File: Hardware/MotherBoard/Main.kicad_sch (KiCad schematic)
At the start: 15 parts, among them J9 Conn_02x02_Odd_Even, SW1 SW_Push, U2 28C256, U3 WD65C22, U4 HM62256BLP, U5 WD65C02, X1 ACO-1MHz

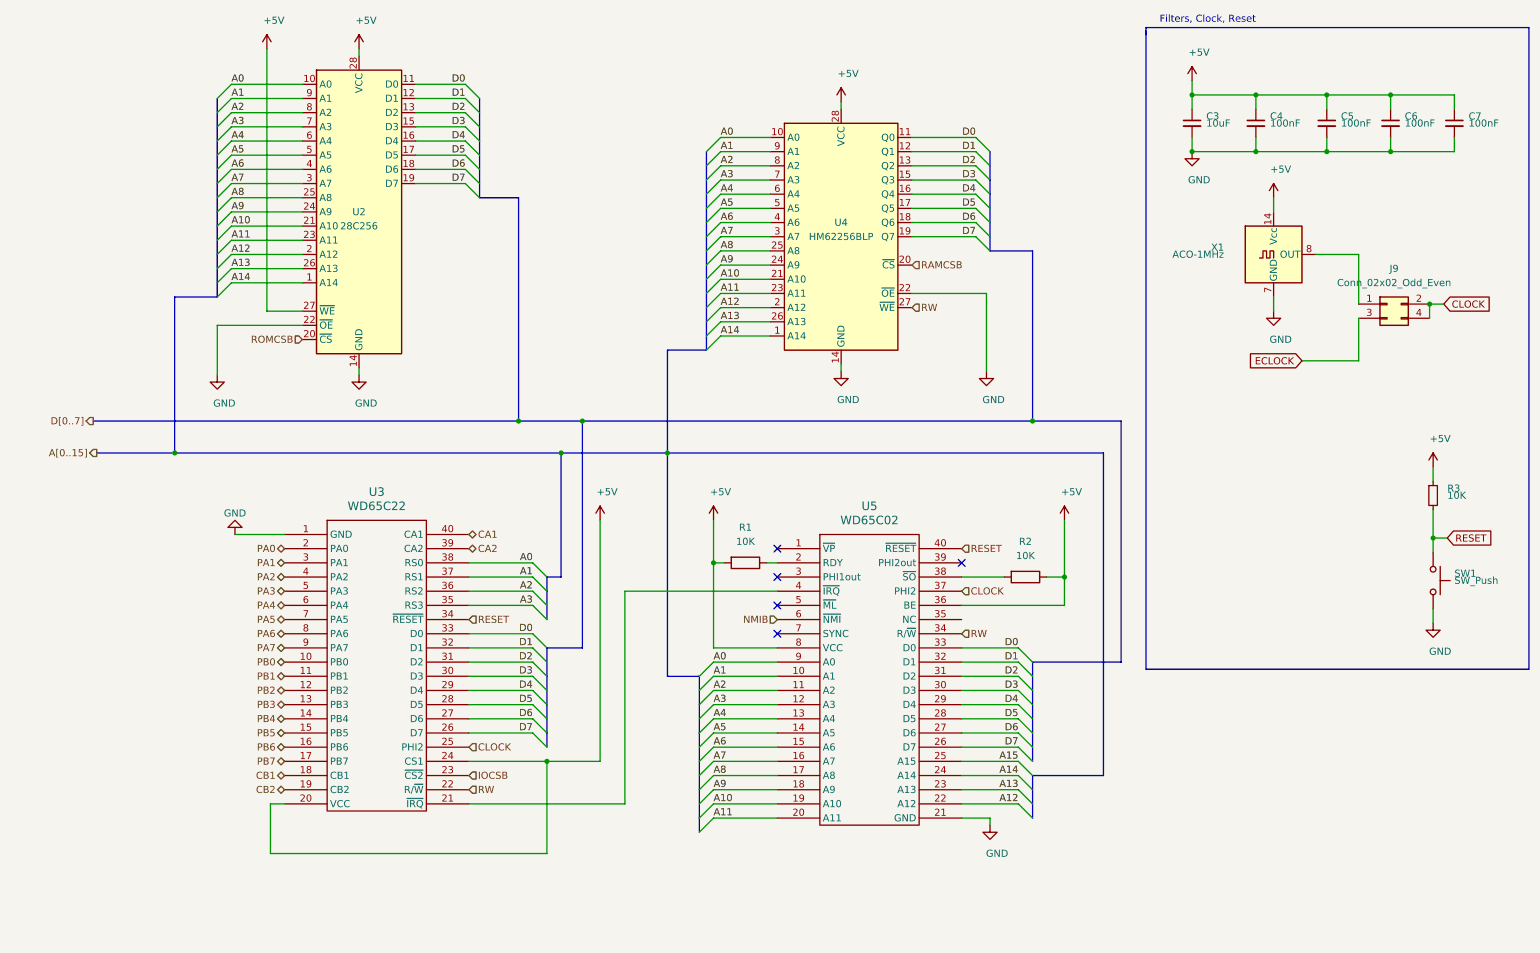
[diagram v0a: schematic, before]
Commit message: Add buffers to extenstion ports
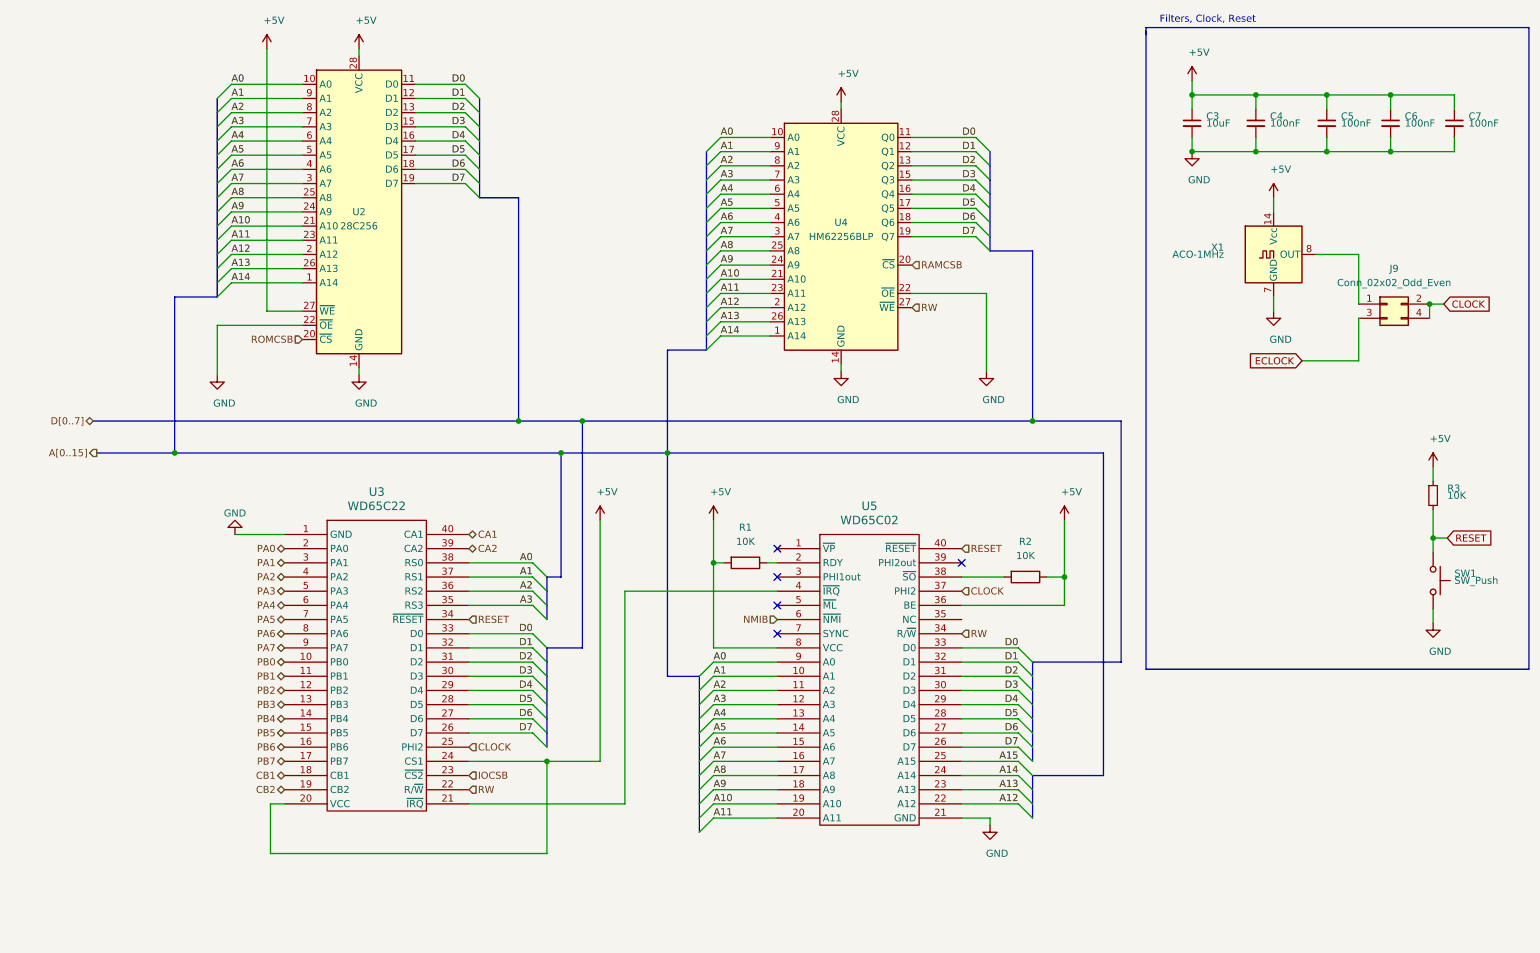
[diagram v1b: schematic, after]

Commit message: Fix
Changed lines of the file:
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@@
   (junction (at 128.905 92.71) (diameter 1.016) (color 0 0 0 0))
   (junction (at 194.31 86.995) (diameter 1.016) (color 0 0 0 0))
+  (no_connect (at 148.59 114.935))
+  (no_connect (at 181.61 112.395))
   (no_connect (at 148.59 125.095))
-  (no_connect (at 181.61 112.395))
   (no_connect (at 148.59 120.015))
   (no_connect (at 148.59 109.855))
-  (no_connect (at 148.59 114.935))
   (bus_entry (at 48.26 29.21) (size 2.54 -2.54)
     (stroke (width 0.1524) (type solid) (color 0 0 0 0))
@@
     (stroke (width 0) (type solid) (color 0 0 0 0))
   )
-  (wire (pts (xy 242.57 76.2) (xy 252.73 76.2))
-    (stroke (width 0) (type solid) (color 0 0 0 0))
-  )
   (wire (pts (xy 245.11 57.15) (xy 252.73 57.15))
     (stroke (width 0) (type solid) (color 0 0 0 0))
@@
     (stroke (width 0) (type solid) (color 0 0 0 0))
   )
+  (wire (pts (xy 252.73 76.2) (xy 267.97 76.2))
+    (stroke (width 0) (type solid) (color 0 0 0 0))
+  )
   (wire (pts (xy 258.445 28.575) (xy 269.875 28.575))
     (stroke (width 0) (type solid) (color 0 0 0 0))
@@
   (label "A12" (at 191.77 155.575 180)
     (effects (font (size 1.27 1.27)) (justify right bottom))
-  )
-  (global_label "ECLOCK" (shape input) (at 242.57 76.2 180)
-    (effects (font (size 1.27 1.27)) (justify right))
-  )
-  (global_label "CLOCK" (shape input) (at 267.97 66.04 0)
-    (effects (font (size 1.27 1.27)) (justify left))
-  )
-  (global_label "RESET" (shape input) (at 268.605 107.95 0)
-    (effects (font (size 1.27 1.27)) (justify left))
   )
   (hierarchical_label "D[0..7]" (shape bidirectional) (at 26.035 86.995 180)
@@
     (effects (font (size 1.27 1.27)) (justify left))
   )
+  (hierarchical_label "CLOCK" (shape input) (at 267.97 66.04 0)
+    (effects (font (size 1.27 1.27)) (justify left))
+  )
+  (hierarchical_label "ECLOCK" (shape input) (at 267.97 76.2 0)
+    (effects (font (size 1.27 1.27)) (justify left))
+  )
+  (hierarchical_label "RESET" (shape input) (at 268.605 107.95 0)
+    (effects (font (size 1.27 1.27)) (justify left))
+  )

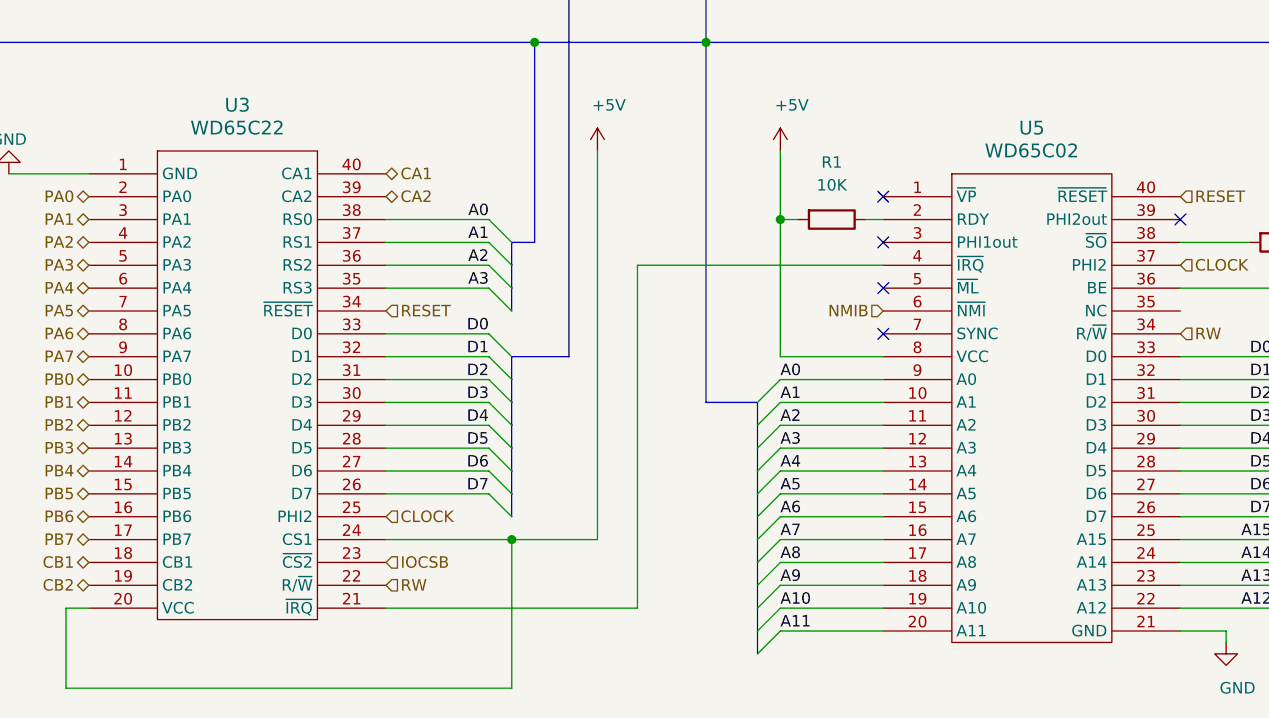
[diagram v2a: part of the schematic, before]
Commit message: Replace logic IC 4xxx by 74hcxx
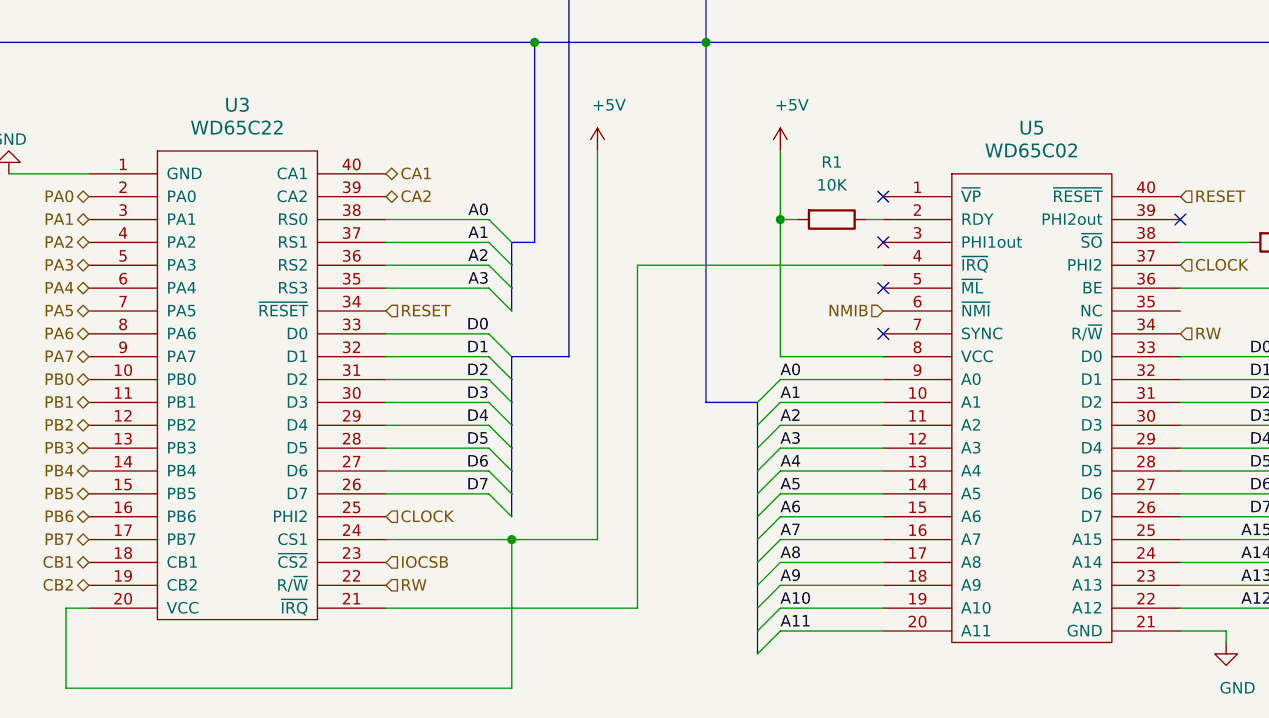
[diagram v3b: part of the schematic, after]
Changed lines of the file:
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@@
   (junction (at 128.905 92.71) (diameter 1.016) (color 0 0 0 0))
   (junction (at 194.31 86.995) (diameter 1.016) (color 0 0 0 0))
+  (no_connect (at 148.59 125.095))
+  (no_connect (at 148.59 109.855))
+  (no_connect (at 181.61 112.395))
   (no_connect (at 148.59 114.935))
-  (no_connect (at 181.61 112.395))
-  (no_connect (at 148.59 125.095))
   (no_connect (at 148.59 120.015))
-  (no_connect (at 148.59 109.855))
   (bus_entry (at 48.26 29.21) (size 2.54 -2.54)
     (stroke (width 0.1524) (type solid) (color 0 0 0 0))

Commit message: Finalize daughter board
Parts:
- added C8: 470nF, Capacitor_THT:C_Disc_D5.0mm_W2.5mm_P2.50mm, symbol Device:C_Small
- SW1: value SW_Push -> RESET_SW
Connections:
- net GND: now also C8.2
- net RESET: now also C8.1
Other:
- moved on the sheet: J9, X1
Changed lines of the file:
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@@
 (kicad_sch (version 20201015) (generator eeschema)
-  (page 1 4)
   (paper "A4")
   (title_block
@@
   (junction (at 258.445 28.575) (diameter 1.016) (color 0 0 0 0))
   (junction (at 258.445 38.735) (diameter 1.016) (color 0 0 0 0))
-  (junction (at 265.43 66.04) (diameter 1.016) (color 0 0 0 0))
   (junction (at 266.065 107.95) (diameter 1.016) (color 0 0 0 0))
+  (junction (at 266.065 121.92) (diameter 1.016) (color 0 0 0 0))
+  (junction (at 266.7 71.755) (diameter 1.016) (color 0 0 0 0))
   (junction (at 40.64 92.71) (diameter 1.016) (color 0 0 0 0))
   (junction (at 102.235 86.995) (diameter 1.016) (color 0 0 0 0))
@@
     (stroke (width 0) (type solid) (color 0 0 0 0))
   )
-  (wire (pts (xy 237.49 46.99) (xy 237.49 49.53))
-    (stroke (width 0) (type solid) (color 0 0 0 0))
-  )
-  (wire (pts (xy 237.49 64.77) (xy 237.49 67.31))
-    (stroke (width 0) (type solid) (color 0 0 0 0))
-  )
-  (wire (pts (xy 245.11 57.15) (xy 252.73 57.15))
+  (wire (pts (xy 238.76 52.705) (xy 238.76 55.245))
+    (stroke (width 0) (type solid) (color 0 0 0 0))
+  )
+  (wire (pts (xy 238.76 70.485) (xy 238.76 73.025))
+    (stroke (width 0) (type solid) (color 0 0 0 0))
+  )
+  (wire (pts (xy 246.38 62.865) (xy 254 62.865))
     (stroke (width 0) (type solid) (color 0 0 0 0))
   )
@@
     (stroke (width 0) (type solid) (color 0 0 0 0))
   )
-  (wire (pts (xy 252.73 57.15) (xy 252.73 66.04))
-    (stroke (width 0) (type solid) (color 0 0 0 0))
-  )
-  (wire (pts (xy 252.73 68.58) (xy 252.73 76.2))
-    (stroke (width 0) (type solid) (color 0 0 0 0))
-  )
-  (wire (pts (xy 252.73 76.2) (xy 267.97 76.2))
+  (wire (pts (xy 254 62.865) (xy 254 71.755))
+    (stroke (width 0) (type solid) (color 0 0 0 0))
+  )
+  (wire (pts (xy 254 74.295) (xy 254 81.915))
+    (stroke (width 0) (type solid) (color 0 0 0 0))
+  )
+  (wire (pts (xy 254 81.915) (xy 269.24 81.915))
+    (stroke (width 0) (type solid) (color 0 0 0 0))
+  )
+  (wire (pts (xy 255.905 107.95) (xy 255.905 113.665))
+    (stroke (width 0) (type solid) (color 0 0 0 0))
+  )
+  (wire (pts (xy 255.905 118.745) (xy 255.905 121.92))
+    (stroke (width 0) (type solid) (color 0 0 0 0))
+  )
+  (wire (pts (xy 255.905 121.92) (xy 266.065 121.92))
     (stroke (width 0) (type solid) (color 0 0 0 0))
   )
@@
     (stroke (width 0) (type solid) (color 0 0 0 0))
   )
-  (wire (pts (xy 265.43 66.04) (xy 265.43 68.58))
-    (stroke (width 0) (type solid) (color 0 0 0 0))
-  )
-  (wire (pts (xy 265.43 66.04) (xy 267.97 66.04))
-    (stroke (width 0) (type solid) (color 0 0 0 0))
-  )
   (wire (pts (xy 266.065 95.25) (xy 266.065 97.79))
     (stroke (width 0) (type solid) (color 0 0 0 0))
@@
     (stroke (width 0) (type solid) (color 0 0 0 0))
   )
+  (wire (pts (xy 266.065 107.95) (xy 255.905 107.95))
+    (stroke (width 0) (type solid) (color 0 0 0 0))
+  )
   (wire (pts (xy 266.065 107.95) (xy 266.065 110.49))
     (stroke (width 0) (type solid) (color 0 0 0 0))
@@
     (stroke (width 0) (type solid) (color 0 0 0 0))
   )
-  (wire (pts (xy 266.065 120.65) (xy 266.065 123.19))
+  (wire (pts (xy 266.065 120.65) (xy 266.065 121.92))
+    (stroke (width 0) (type solid) (color 0 0 0 0))
+  )
+  (wire (pts (xy 266.065 121.92) (xy 266.065 123.19))
+    (stroke (width 0) (type solid) (color 0 0 0 0))
+  )
+  (wire (pts (xy 266.7 71.755) (xy 266.7 74.295))
+    (stroke (width 0) (type solid) (color 0 0 0 0))
+  )
+  (wire (pts (xy 266.7 71.755) (xy 269.24 71.755))
     (stroke (width 0) (type solid) (color 0 0 0 0))
   )
@@
     (effects (font (size 1.27 1.27)) (justify left))
   )
-  (hierarchical_label "CLOCK" (shape input) (at 267.97 66.04 0)
-    (effects (font (size 1.27 1.27)) (justify left))
-  )
-  (hierarchical_label "ECLOCK" (shape input) (at 267.97 76.2 0)
-    (effects (font (size 1.27 1.27)) (justify left))
-  )
   (hierarchical_label "RESET" (shape input) (at 268.605 107.95 0)
     (effects (font (size 1.27 1.27)) (justify left))
   )
+  (hierarchical_label "CLOCK" (shape input) (at 269.24 71.755 0)
+    (effects (font (size 1.27 1.27)) (justify left))
+  )
+  (hierarchical_label "ECLOCK" (shape input) (at 269.24 81.915 0)
+    (effects (font (size 1.27 1.27)) (justify left))
+  )
   (symbol (lib_id "power:+5V") (at 57.15 20.32 0) (unit 1)
     (in_bom yes) (on_board yes)
@@
     )
   )
-  (symbol (lib_id "power:+5V") (at 237.49 46.99 0) (unit 1)
-    (in_bom yes) (on_board yes)
-    (property "Reference" "#PWR0116" (id 0) (at 237.49 50.8 0)
-      (effects (font (size 1.27 1.27)) hide)
-    )
-    (property "Value" "+5V" (id 1) (at 238.76 41.91 0))
-    (property "Footprint" "" (id 2) (at 237.49 46.99 0)
-      (effects (font (size 1.27 1.27)) hide)
-    )
-    (property "Datasheet" "" (id 3) (at 237.49 46.99 0)
+  (symbol (lib_id "power:+5V") (at 238.76 52.705 0) (unit 1)
+    (in_bom yes) (on_board yes)
+    (property "Reference" "#PWR0116" (id 0) (at 238.76 56.515 0)
+      (effects (font (size 1.27 1.27)) hide)
+    )
+    (property "Value" "+5V" (id 1) (at 240.03 47.625 0))
+    (property "Footprint" "" (id 2) (at 238.76 52.705 0)
+      (effects (font (size 1.27 1.27)) hide)
+    )
+    (property "Datasheet" "" (id 3) (at 238.76 52.705 0)
       (effects (font (size 1.27 1.27)) hide)
     )
@@
     )
   )
-  (symbol (lib_id "power:GND") (at 237.49 67.31 0) (unit 1)
-    (in_bom yes) (on_board yes)
-    (property "Reference" "#PWR0117" (id 0) (at 237.49 73.66 0)
-      (effects (font (size 1.27 1.27)) hide)
-    )
-    (property "Value" "GND" (id 1) (at 238.76 72.39 0))
-    (property "Footprint" "" (id 2) (at 237.49 67.31 0)
-      (effects (font (size 1.27 1.27)) hide)
-    )
-    (property "Datasheet" "" (id 3) (at 237.49 67.31 0)
+  (symbol (lib_id "power:GND") (at 238.76 73.025 0) (unit 1)
+    (in_bom yes) (on_board yes)
+    (property "Reference" "#PWR0117" (id 0) (at 238.76 79.375 0)
+      (effects (font (size 1.27 1.27)) hide)
+    )
+    (property "Value" "GND" (id 1) (at 240.03 78.105 0))
+    (property "Footprint" "" (id 2) (at 238.76 73.025 0)
+      (effects (font (size 1.27 1.27)) hide)
+    )
+    (property "Datasheet" "" (id 3) (at 238.76 73.025 0)
       (effects (font (size 1.27 1.27)) hide)
     )
@@
     )
   )
+  (symbol (lib_id "Device:C_Small") (at 255.905 116.205 0) (unit 1)
+    (in_bom yes) (on_board yes)
+    (property "Reference" "C8" (id 0) (at 259.08 114.3 0)
+      (effects (font (size 1.27 1.27)) (justify left))
+    )
+    (property "Value" "470nF" (id 1) (at 259.08 116.84 0)
+      (effects (font (size 1.27 1.27)) (justify left))
+    )
+    (property "Footprint" "Capacitor_THT:C_Disc_D5.0mm_W2.5mm_P2.50mm" (id 2) (at 255.905 116.205 0)
+      (effects (font (size 1.27 1.27)) hide)
+    )
+    (property "Datasheet" "~" (id 3) (at 255.905 116.205 0)
+      (effects (font (size 1.27 1.27)) hide)
+    )
+  )
   (symbol (lib_id "Device:C_Small") (at 258.445 33.655 0) (unit 1)
     (in_bom yes) (on_board yes)
@@
   (symbol (lib_id "Switch:SW_Push") (at 266.065 115.57 270) (unit 1)
     (in_bom yes) (on_board yes)
-    (property "Reference" "SW1" (id 0) (at 269.875 114.3 90)
+    (property "Reference" "SW1" (id 0) (at 269.875 113.665 90)
       (effects (font (size 1.27 1.27)) (justify left))
     )
-    (property "Value" "SW_Push" (id 1) (at 269.875 115.57 90)
+    (property "Value" "RESET_SW" (id 1) (at 269.875 116.205 90)
       (effects (font (size 1.27 1.27)) (justify left))
     )
@@
     )
   )
-  (symbol (lib_id "Connector_Generic:Conn_02x02_Odd_Even") (at 257.81 66.04 0) (unit 1)
-    (in_bom yes) (on_board yes)
-    (property "Reference" "J9" (id 0) (at 259.08 59.69 0))
-    (property "Value" "Conn_02x02_Odd_Even" (id 1) (at 259.08 62.23 0))
-    (property "Footprint" "Connector_PinHeader_2.54mm:PinHeader_2x02_P2.54mm_Vertical" (id 2) (at 257.81 66.04 0)
-      (effects (font (size 1.27 1.27)) hide)
-    )
-    (property "Datasheet" "~" (id 3) (at 257.81 66.04 0)
-      (effects (font (size 1.27 1.27)) hide)
-    )
-  )
-  (symbol (lib_id "Oscillator:ACO-xxxMHz") (at 237.49 57.15 0) (unit 1)
-    (in_bom yes) (on_board yes)
-    (property "Reference" "X1" (id 0) (at 228.6 55.88 0)
+  (symbol (lib_id "Connector_Generic:Conn_02x02_Odd_Even") (at 259.08 71.755 0) (unit 1)
+    (in_bom yes) (on_board yes)
+    (property "Reference" "J9" (id 0) (at 260.35 65.405 0))
+    (property "Value" "Conn_02x02_Odd_Even" (id 1) (at 260.35 67.945 0))
+    (property "Footprint" "Connector_PinHeader_2.54mm:PinHeader_2x02_P2.54mm_Vertical" (id 2) (at 259.08 71.755 0)
+      (effects (font (size 1.27 1.27)) hide)
+    )
+    (property "Datasheet" "~" (id 3) (at 259.08 71.755 0)
+      (effects (font (size 1.27 1.27)) hide)
+    )
+  )
+  (symbol (lib_id "Oscillator:ACO-xxxMHz") (at 238.76 62.865 0) (unit 1)
+    (in_bom yes) (on_board yes)
+    (property "Reference" "X1" (id 0) (at 229.87 61.595 0)
       (effects (font (size 1.27 1.27)) (justify right))
     )
-    (property "Value" "ACO-1MHz" (id 1) (at 228.6 57.15 0)
+    (property "Value" "ACO-1MHz" (id 1) (at 229.87 63.5 0)
       (effects (font (size 1.27 1.27)) (justify right))
     )
-    (property "Footprint" "Oscillator:Oscillator_DIP-14" (id 2) (at 248.92 66.04 0)
-      (effects (font (size 1.27 1.27)) hide)
-    )
-    (property "Datasheet" "http://www.conwin.com/datasheets/cx/cx030.pdf" (id 3) (at 234.95 57.15 0)
-      (effects (font (size 1.27 1.27)) hide)
-    )
+    (property "Footprint" "Oscillator:Oscillator_DIP-14" (id 2) (at 250.19 71.755 0)
+      (effects (font (size 1.27 1.27)) hide)
+    )
+    (property "Datasheet" "http://www.conwin.com/datasheets/cx/cx030.pdf" (id 3) (at 236.22 62.865 0)
+      (effects (font (size 1.27 1.27)) hide)
+    )
